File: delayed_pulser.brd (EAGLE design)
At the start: 160 x 100 mm, 36 parts, among them T1 2N2369, U1 MC100EP196FAG, U2 MC100EPT22DG, U3 MC100EPT22DG, X1 BU-SMA-H, X2 BU-SMA-H, X3 BU-SMA-H, X4 BU-SMA-H

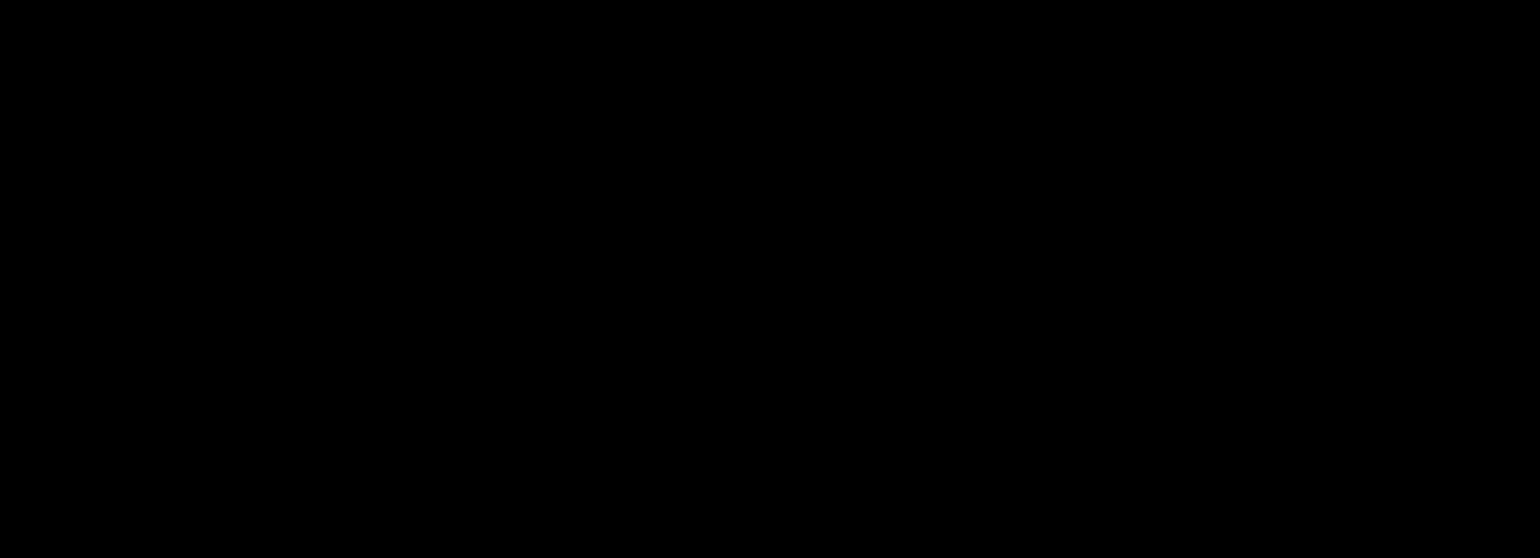
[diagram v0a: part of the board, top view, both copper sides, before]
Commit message: added delayed pulse generator, only avalanche transistor for now
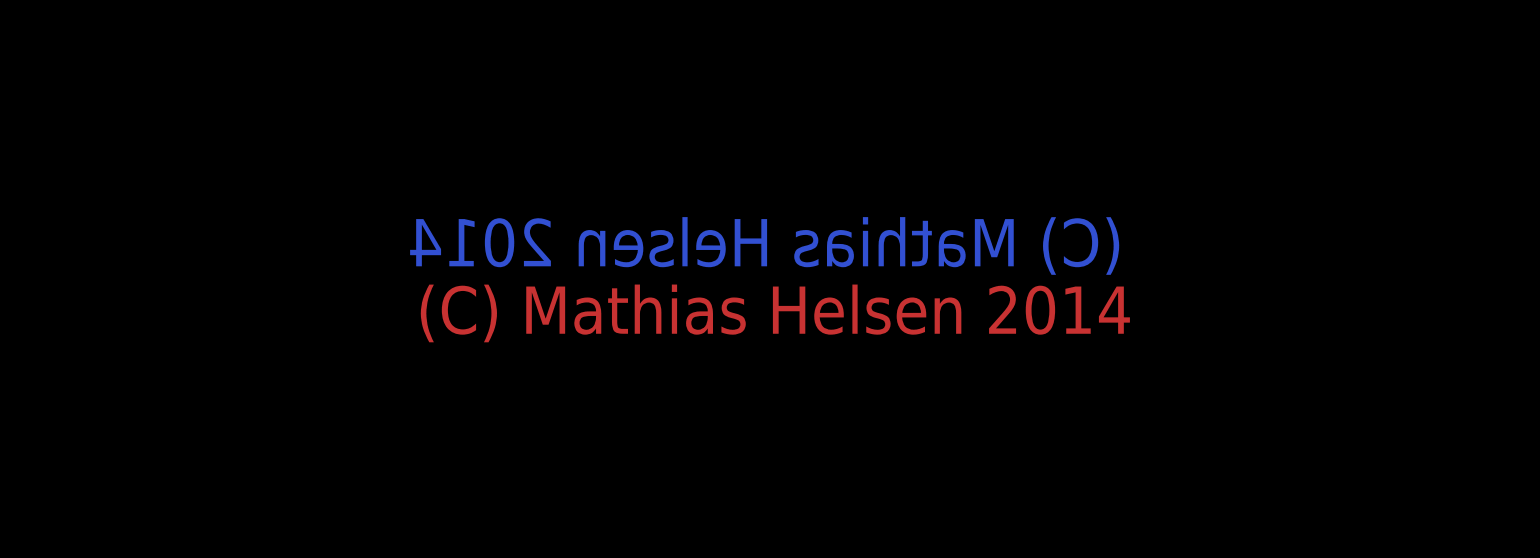
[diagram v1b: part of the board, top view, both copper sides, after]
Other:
- board text added: "(C) Mathias Helsen 2014"
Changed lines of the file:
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@@
 <wire x1="160" y1="100" x2="0" y2="100" width="0" layer="20"/>
 <wire x1="0" y1="100" x2="0" y2="0" width="0" layer="20"/>
+<text x="44.45" y="64.77" size="1.778" layer="16" rot="MR0">(C) Mathias Helsen 2014</text>
+<text x="17.78" y="62.23" size="1.778" layer="1">(C) Mathias Helsen 2014</text>
 </plain>
 <attributes>

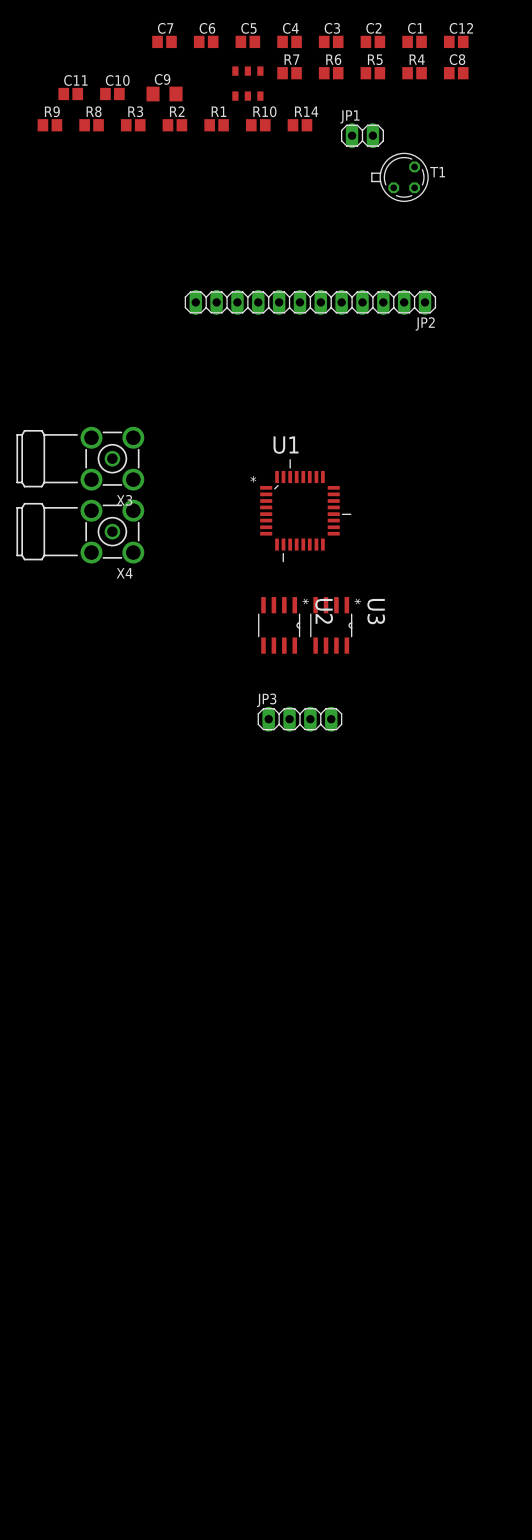
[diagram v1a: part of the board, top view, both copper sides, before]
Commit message: added HV supply
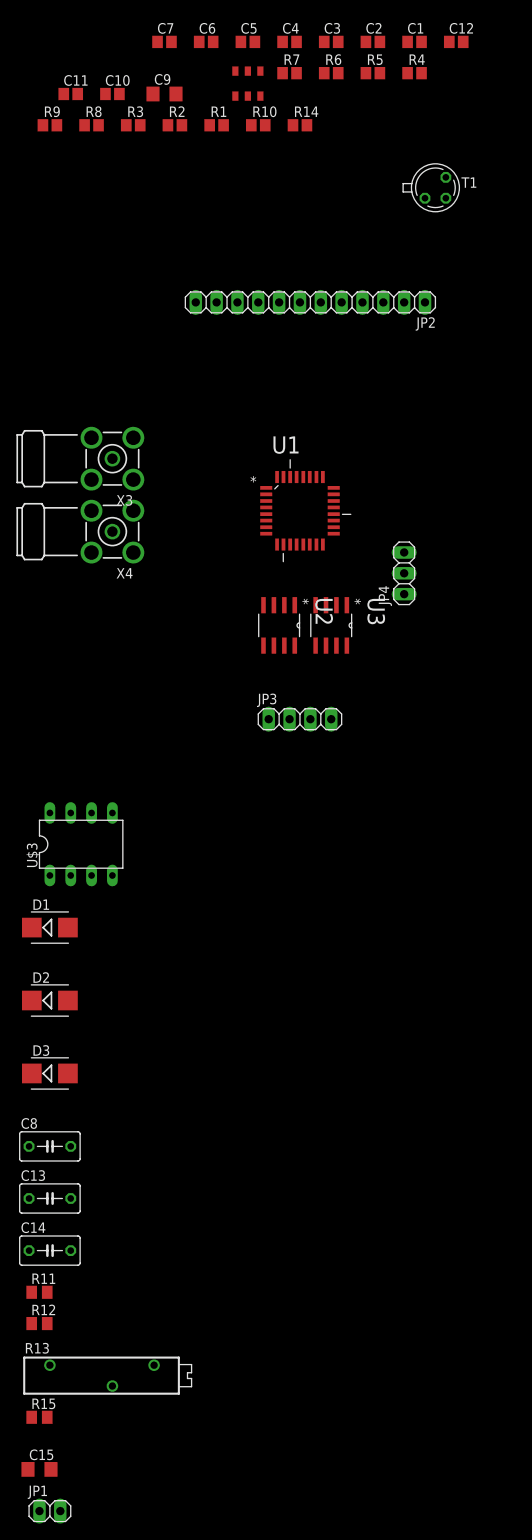
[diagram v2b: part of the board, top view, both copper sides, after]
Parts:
- added C13, C14: 0.47, resistor:C050-035X075
- added C15: (no value), resistor:C1206
- added D1, D2, D3: ES2D, diode:SMB
- added JP4: (no value), pinhead:1X03
- added R11: 1M, resistor:M0805
- added R12: (no value), resistor:M0805
- added R13: (no value), resistor:RTRIMT18
- added R15: 220, resistor:M0805
- added U$3: LT1073, LT1073:DIL08
- C11, C12: value (none) -> 8p
- C8: value 4p8 -> 0.47; device resistor:C0805 -> resistor:C050-035X075
- R14: value Rlim -> 10k
- R3: value 100 -> 200
- R5, R6: value 30 -> 50
- moved JP1 171.9 mm to (-66.0, -110.5)
- moved C8 139.9 mm to (-66.0, -66.0)
- moved T1 4.02 mm to (-19.1, 50.8)
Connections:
- new net N$37: C14.2, D1.A, U$3.3
- new net N$38: R12.2, R13.1
- new net N$39: R11.1, R13.3
- new net N$40: R13.2, U$3.8
- new net N$41: R15.1, U$3.1
- net +3V3: now also C15.1, JP4.2, R15.2, U$3.2
- net GND: now also C13.2, C15.2, C8.2, JP1.2, JP4.1, JP4.3, R12.1, R5.1, R6.2, U$3.4, U$3.5; no longer JP1.1
- net N$11: now also C11.1; no longer C8.2, R5.2
- net N$12: now also C12.1; no longer R6.2
- net N$13: now also C8.1, D1.C, D2.A; no longer JP1.2, R14.2
- net N$24: now also C14.1, D2.C, D3.A; no longer C11.1, R5.1
- net N$25: now also C13.1, D3.C, JP1.1, R11.2, R14.2; no longer C12.1, R6.1
- net N$26: now also R5.2
- net N$27: now also R6.1
- net N$7: no longer C8.1

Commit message: added comment
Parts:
- R12: value (none) -> 2k4
- R13: value (none) -> 10k
- moved JP4 9.16 mm to (-15.2, 8.89)
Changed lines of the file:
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@@
 </element>
 <element name="JP3" library="pinhead" package="1X04" value="" x="-35.56" y="-13.97"/>
-<element name="JP4" library="pinhead" package="1X03" value="" x="-22.86" y="3.81" rot="R90"/>
+<element name="JP4" library="pinhead" package="1X03" value="" x="-15.24" y="8.89" rot="R90"/>
 <element name="U$3" library="LT1073" package="DIL08" value="LT1073" x="-62.23" y="-29.21"/>
 <element name="D1" library="diode" package="SMB" value="ES2D" x="-66.04" y="-39.37"/>
@@
 <element name="C14" library="resistor" package="C050-035X075" value="0.47" x="-66.04" y="-78.74"/>
 <element name="R11" library="resistor" package="M0805" value="1M" x="-67.31" y="-83.82"/>
-<element name="R12" library="resistor" package="M0805" value="" x="-67.31" y="-87.63"/>
-<element name="R13" library="resistor" package="RTRIMT18" value="" x="-58.42" y="-93.98"/>
+<element name="R12" library="resistor" package="M0805" value="2k4" x="-67.31" y="-87.63"/>
+<element name="R13" library="resistor" package="RTRIMT18" value="10k" x="-58.42" y="-93.98"/>
 <element name="R15" library="resistor" package="M0805" value="220" x="-67.31" y="-99.06"/>
 <element name="C15" library="resistor" package="C1206" value="" x="-67.31" y="-105.41"/>
@@
 <wire x1="-35.1536" y1="15.5448" x2="-39.6748" y2="9.4234" width="0" layer="19" extent="1-1"/>
 <wire x1="-31.4452" y1="14.224" x2="-35.1536" y2="15.5448" width="0" layer="19" extent="1-1"/>
-<wire x1="-22.86" y1="6.35" x2="-31.4452" y2="14.224" width="0" layer="19" extent="1-1"/>
-<wire x1="-22.86" y1="1.27" x2="-22.86" y2="6.35" width="0" layer="19" extent="1-1"/>
 <wire x1="-55.8701" y1="11.4399" x2="-39.6748" y2="9.4234" width="0" layer="19" extent="1-1"/>
 <wire x1="-55.8701" y1="15.2301" x2="-55.8701" y2="11.4399" width="0" layer="19" extent="1-1"/>
@@
 <wire x1="-60.9699" y1="20.3299" x2="-60.9699" y2="15.2301" width="0" layer="19" extent="1-1"/>
 <wire x1="-55.8701" y1="20.3299" x2="-55.8701" y2="15.2301" width="0" layer="19" extent="1-1"/>
+<wire x1="-15.24" y1="11.43" x2="-31.4452" y2="14.224" width="0" layer="19" extent="1-1"/>
+<wire x1="-15.24" y1="6.35" x2="-15.24" y2="11.43" width="0" layer="19" extent="1-1"/>
 <wire x1="-48.26" y1="36.83" x2="-55.8701" y2="20.3299" width="0" layer="19" extent="1-1"/>
 <wire x1="-46.57" y1="58.42" x2="-48.26" y2="36.83" width="0" layer="19" extent="1-1"/>
@@
 <wire x1="-22.44" y1="64.77" x2="-27.52" y2="64.77" width="0" layer="19" extent="1-1"/>
 <wire x1="-20.74" y1="68.58" x2="-22.44" y2="64.77" width="0" layer="19" extent="1-1"/>
-<wire x1="16.5001" y1="16.5001" x2="-22.86" y2="6.35" width="0" layer="19" extent="1-1"/>
+<wire x1="16.5001" y1="16.5001" x2="-15.24" y2="11.43" width="0" layer="19" extent="1-1"/>
 <wire x1="19.05" y1="19.05" x2="16.5001" y2="16.5001" width="0" layer="19" extent="1-1"/>
 <wire x1="21.5999" y1="21.5999" x2="19.05" y2="19.05" width="0" layer="19" extent="1-1"/>
@@
 <wire x1="-36.195" y1="-5.0038" x2="-63.5" y2="-33.02" width="0" layer="19" extent="1-1"/>
 <wire x1="-29.845" y1="-5.0038" x2="-36.195" y2="-5.0038" width="0" layer="19" extent="1-1"/>
-<wire x1="-22.86" y1="3.81" x2="-29.845" y2="-5.0038" width="0" layer="19" extent="1-1"/>
-<wire x1="-31.4452" y1="9.4234" x2="-22.86" y2="3.81" width="0" layer="19" extent="1-1"/>
+<wire x1="-35.1536" y1="7.3152" x2="-36.195" y2="-5.0038" width="0" layer="19" extent="1-1"/>
+<wire x1="-31.4452" y1="9.4234" x2="-35.1536" y2="7.3152" width="0" layer="19" extent="1-1"/>
 <wire x1="-31.4452" y1="10.2362" x2="-31.4452" y2="9.4234" width="0" layer="19" extent="1-1"/>
 <wire x1="-31.4452" y1="12.6238" x2="-31.4452" y2="10.2362" width="0" layer="19" extent="1-1"/>
-<wire x1="-35.1536" y1="7.3152" x2="-31.4452" y2="9.4234" width="0" layer="19" extent="1-1"/>
+<wire x1="-15.24" y1="8.89" x2="-31.4452" y2="9.4234" width="0" layer="19" extent="1-1"/>
 <wire x1="-53.47" y1="62.23" x2="-31.4452" y2="12.6238" width="0" layer="19" extent="1-1"/>
 <wire x1="-52.92" y1="68.58" x2="-53.47" y2="62.23" width="0" layer="19" extent="1-1"/>

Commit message: bla
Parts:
- C13, C14, C8: value 0.47 -> (none); device resistor:C050-035X075 -> resistor:C0805K
- moved X2 39.0 mm to (0.00, -15.0)
- moved U$2 33.5 mm to (-2.54, 0.00)
- moved C14 29.6 mm to (-61.0, -49.5)
- moved C13 28.4 mm to (-61.0, -44.5)
- moved X1 27.1 mm to (0.00, 15.0)
- moved C8 25.0 mm to (-72.4, -41.9), turned to 90 degrees
- moved X4 23.9 mm to (-58.4, -15.0)
- moved U2 17.3 mm to (-48.3, -16.5)
- moved U1 17.1 mm to (-48.3, 0.00)
- moved U3 16.6 mm to (-40.6, -16.5)
- moved JP2 15.3 mm to (-40.6, 22.9)
- moved JP3 14.5 mm to (-44.5, -25.4)
- moved D3 7.73 mm to (-67.3, -49.5), turned to 180 degrees
- moved D2 4.02 mm to (-67.3, -44.5)
- moved U$3 2.84 mm to (-64.8, -30.5)
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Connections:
- net GND: now also C14.2; no longer C8.2
- net N$13: now also C13.1; no longer C8.1
- net N$24: now also C8.1; no longer C14.1
- net N$25: now also C14.1; no longer C13.1
- net N$37: now also C8.2; no longer C14.2
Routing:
- net N$24: track 0.00 -> 9.50 mm
- net N$13: track 0.00 -> 8.23 mm
- net N$37: track 0.00 -> 4.42 mm
- net N$25: track 0.00 -> 3.15 mm

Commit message: finished artwork
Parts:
- removed C14: (no value), resistor:C0805K
- removed C15: (no value), resistor:C1206
- removed D1, D2, D3: ES2D, diode:SMB
- removed R11: 1M, resistor:M0805
- removed R12: 2k4, resistor:M0805
- removed R13: 10k, resistor:RTRIMT18
- removed R15: 220, resistor:M0805
- removed U$2: JA4220, \cct:T
- removed U$3: LT1073, LT1073:DIL08
- removed U3: MC100EPT22DG, MC100EPT22:SOIC127P600X175-8N
- added C16, C17: 100p, resistor:C0603
- added C18, C19: (no value), resistor:C0805
- added R16: 50, resistor:R0805
- C11, C12: value 8p -> 8p2; device resistor:C0805 -> resistor:C0603
- C13, C8: device resistor:C0805K -> resistor:C0805
- JP3: device pinhead:1X04 -> pinhead:1X01
- R5, R6: device resistor:R0805 -> resistor:R0603
- moved JP1 153.2 mm to (24.1, 13.3), turned to 180 degrees
- moved C11 110.1 mm to (28.6, 1.91)
- moved R8 106.9 mm to (25.5, -4.45), turned to 90 degrees
- moved R9 106.2 mm to (25.5, 4.45), turned to 90 degrees
- moved C9 104.7 mm to (8.89, -22.9), flipped to the bottom
- moved C10 98.5 mm to (22.0, 5.40), turned to 180 degrees
- moved R3 98.1 mm to (19.8, -4.13)
- moved R6 92.2 mm to (30.9, -2.86), turned to 270 degrees
- moved C7 92.0 mm to (0.00, -7.30), turned to 270 degrees
- moved C6 90.5 mm to (5.08, -5.40), turned to 270 degrees
- moved C4 90.1 mm to (19.8, -1.59)
- moved R2 87.4 mm to (10.5, -3.81), turned to 180 degrees
- moved C5 87.0 mm to (7.30, -3.17), turned to 270 degrees
- moved U$1 85.3 mm to (15.0, 0.00), turned to 180 degrees
- moved R5 84.7 mm to (31.2, 2.86), turned to 270 degrees
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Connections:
- removed net N$13: C13.1, D1.C, D2.A
- removed net N$23: U1.11, U2.1
- removed net N$24: C8.1, D2.C, D3.A
- removed net N$25: C14.1, D3.C, JP1.1, R11.2, R14.2
- removed net N$28: U1.12, U3.3
- removed net N$29: U1.16, U3.1
- removed net N$33: JP3.2, U2.7
- removed net N$35: JP3.4, U3.7
- removed net N$36: JP3.3, U3.6
- removed net N$37: C8.2, D1.A, U$3.3
- removed net N$38: R12.2, R13.1
- removed net N$39: R11.1, R13.3
- removed net N$40: R13.2, U$3.8
- removed net N$41: R15.1, U$3.1
- new net VBB: C13.1, C18.1, C19.1, R10.1, R16.1, R7.1, U1.6
- net +3V3: now also C8.1; no longer C15.1, R15.2, U$3.2, U3.8
- net GND: now also C16.2, C17.2, C18.2, C19.2, C8.2, U$1.P$4, U2.7; no longer C14.2, C15.2, R12.1, U$1.P$1, U$2.P$1, U$2.P$2, U$3.4, U$3.5, U3.5
- net N$22: now also JP1.1, R14.2; no longer R10.1, R7.1, U1.6
- net N$26: now also C16.1; no longer U$2.P$3
- net N$27: now also C17.1; no longer U$2.P$4
- net N$32: now also R16.2
- net N$4: now also U$1.P$2; no longer U$1.P$3
- net N$5: now also U$1.P$3; no longer U$1.P$4
- net N$6: now also U$1.P$1; no longer U$1.P$2
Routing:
- net GND: track 0.00 -> 89.3 mm, vias 0 -> 8
- net +3V3: track 0.00 -> 58.5 mm, vias 0 -> 5
- net VBB: track 0.00 -> 35.9 mm, vias 0 -> 3
- net N$9: track 0.00 -> 34.9 mm, vias 0 -> 1
- net N$1: track 0.00 -> 26.3 mm
- net N$8: track 0.00 -> 23.0 mm
- net N$10: track 0.00 -> 22.3 mm
- net N$14: track 0.00 -> 21.6 mm
- net N$21: track 0.00 -> 21.6 mm
- net N$31: track 0.00 -> 21.4 mm
- net N$15: track 0.00 -> 21.2 mm
- net N$30: track 0.00 -> 21.2 mm
- net N$16: track 0.00 -> 20.5 mm
- net N$20: track 0.00 -> 19.9 mm
- net N$17: track 0.00 -> 19.8 mm
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- added copper zone on layer 1, net GND
- added copper zone on layer 16, net GND
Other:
- board size 160 x 100 mm -> 71.1 x 60 mm
